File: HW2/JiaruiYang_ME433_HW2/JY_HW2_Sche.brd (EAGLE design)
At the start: 50 x 50 mm, 22 parts, among them J1 USB-MB-H

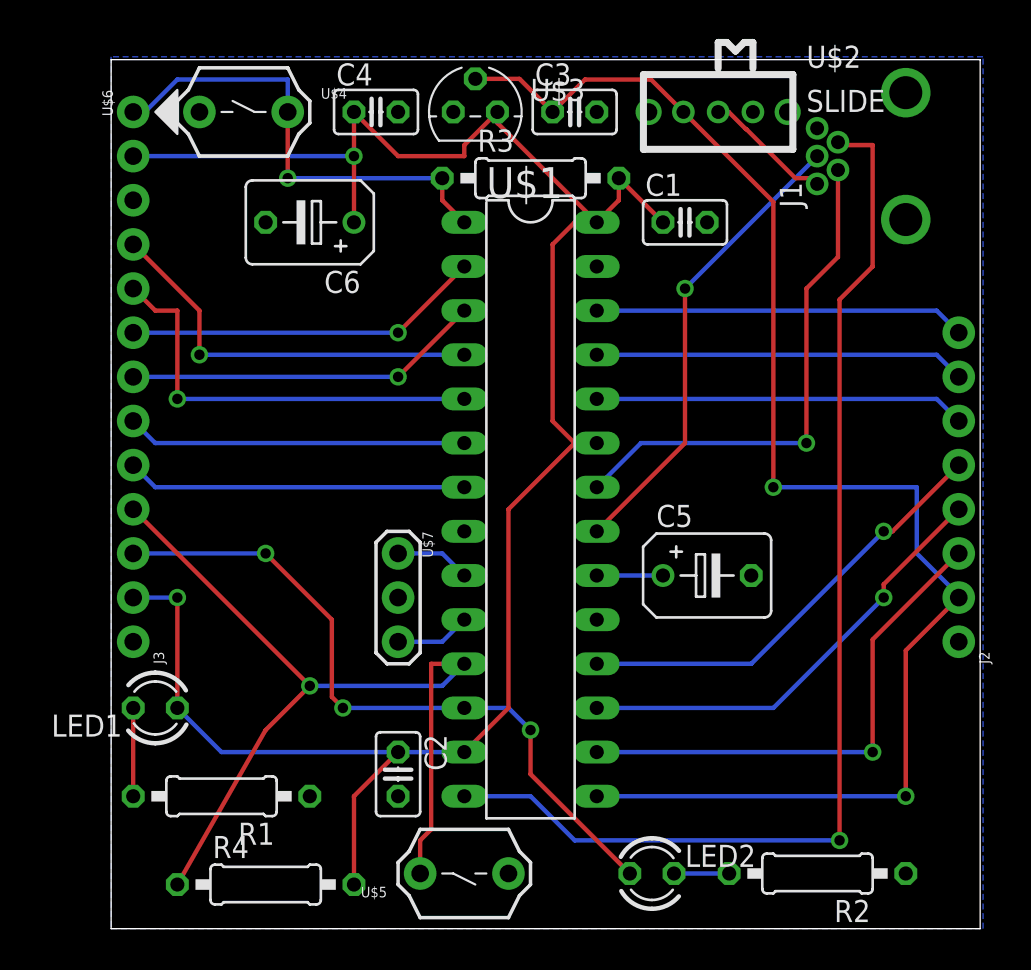
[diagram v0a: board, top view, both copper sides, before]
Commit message: change lable font size
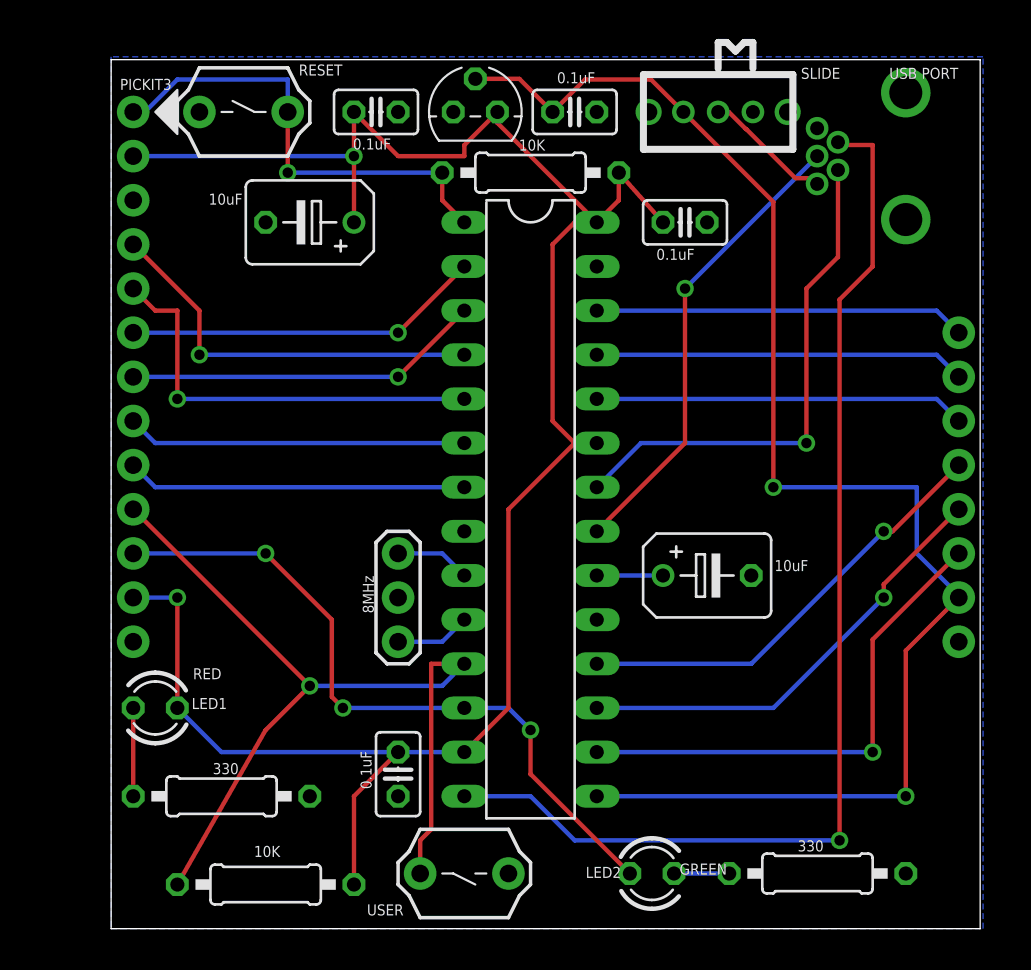
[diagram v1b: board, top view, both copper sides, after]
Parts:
- moved R3 0.32 mm to (24.1, 43.5)
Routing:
- net +3V3: track 117.0 -> 117.5 mm
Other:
- board text added: "USB PORT"
